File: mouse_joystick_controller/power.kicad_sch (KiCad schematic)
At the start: 5 parts, among them J3 5.5x2.5_SMD_RA, J4 5.5x2.1_SMD_RA

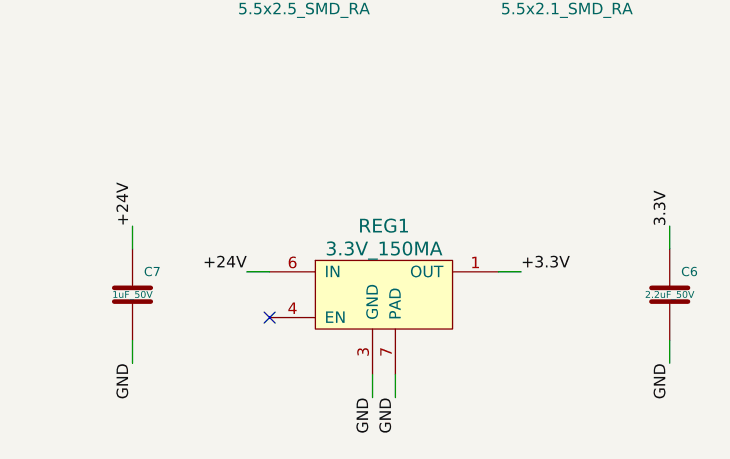
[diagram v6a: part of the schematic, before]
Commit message: Add DDS chip in audio sheet
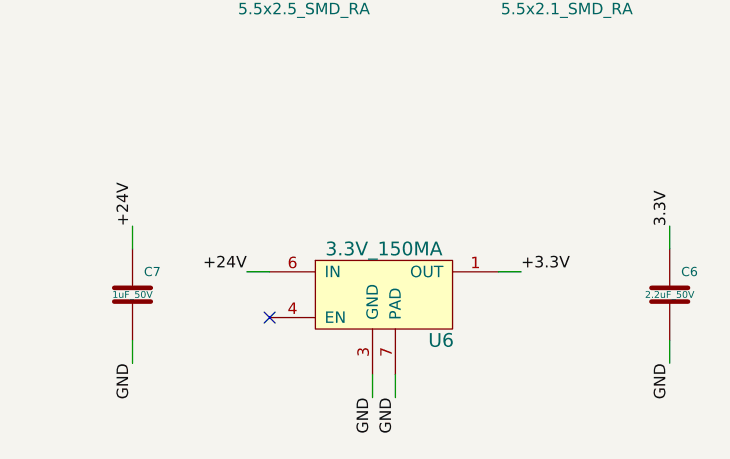
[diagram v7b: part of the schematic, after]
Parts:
- removed REG1: 3.3V_150MA, Janelia:SON65P200X200X80-7N, symbol Janelia:CONV_DC_DC_3.3V_150MA
- added U6: 3.3V_150MA, Janelia:SON65P200X200X80-7N, symbol Janelia:Regulator_Linear_3.3V_150MA_30Vin
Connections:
- net +24V: now also U6.6 (IN)
- net +3.3V: now also U6.1 (OUT)
- net GND: now also U6.3 (GND), U6.7 (PAD)
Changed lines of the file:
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@@
   (title_block
     (title "mouse_joystick_controller")
-    (date "2023-06-02")
+    (date "2023-06-06")
     (rev "2.0")
     (company "Howard Hughes Medical Institute")
@@
     )
   )
-  (symbol (lib_id "Janelia:CONV_DC_DC_3.3V_150MA") (at 163.83 93.98 0) (unit 1)
-    (in_bom yes) (on_board yes) (dnp no) (fields_autoplaced)
-    (property "Reference" "REG1" (at 163.83 88.9 0)
+  (symbol (lib_id "Janelia:Regulator_Linear_3.3V_150MA_30Vin") (at 163.83 93.98 0) (unit 1)
+    (in_bom yes) (on_board yes) (dnp no)
+    (property "Reference" "U6" (at 170.18 101.6 0)
       (effects (font (size 1.524 1.524)))
     )
@@
     (instances
       (project "mouse_joystick_controller"
-        (path "/cc457ebc-4af6-4663-b19f-8cb38f061cb4"
-          (reference "REG1") (unit 1)
-        )
-        (path "/cc457ebc-4af6-4663-b19f-8cb38f061cb4/f62b8726-10b6-4dce-a8d7-bdccf22557c3"
-          (reference "REG1") (unit 1)
-        )
-      )
+        (path "/cc457ebc-4af6-4663-b19f-8cb38f061cb4/f62b8726-10b6-4dce-a8d7-bdccf22557c3"
+          (reference "U6") (unit 1)
+        )
+      )
